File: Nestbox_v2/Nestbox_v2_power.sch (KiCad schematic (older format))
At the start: 27 parts, among them J201 BATT_CONN_01X02, Q201 Q_PMOS_DGS, U201 TPS62745, U202 LTC3534, U203 LP5907

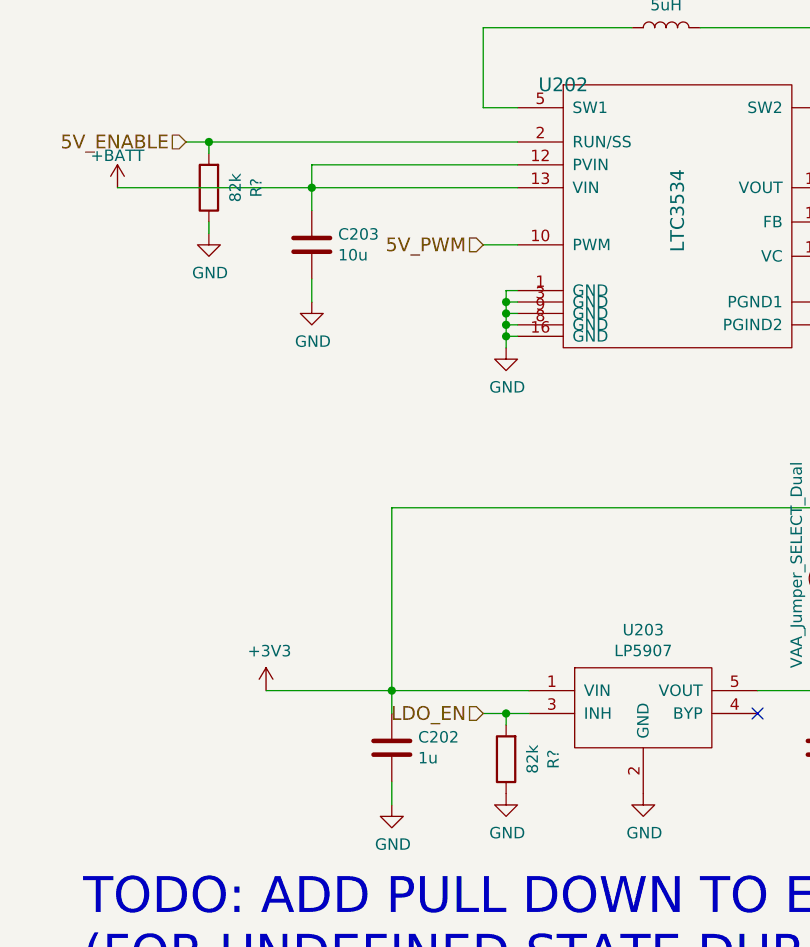
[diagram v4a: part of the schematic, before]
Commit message: TAPEOUT second batch nestbox main + EM pcb. added pull-ups, corrected pmos of load cell, WIFI AND SDCARD ENABLE PMOS ARE STILL WRONGLY ORIENTED
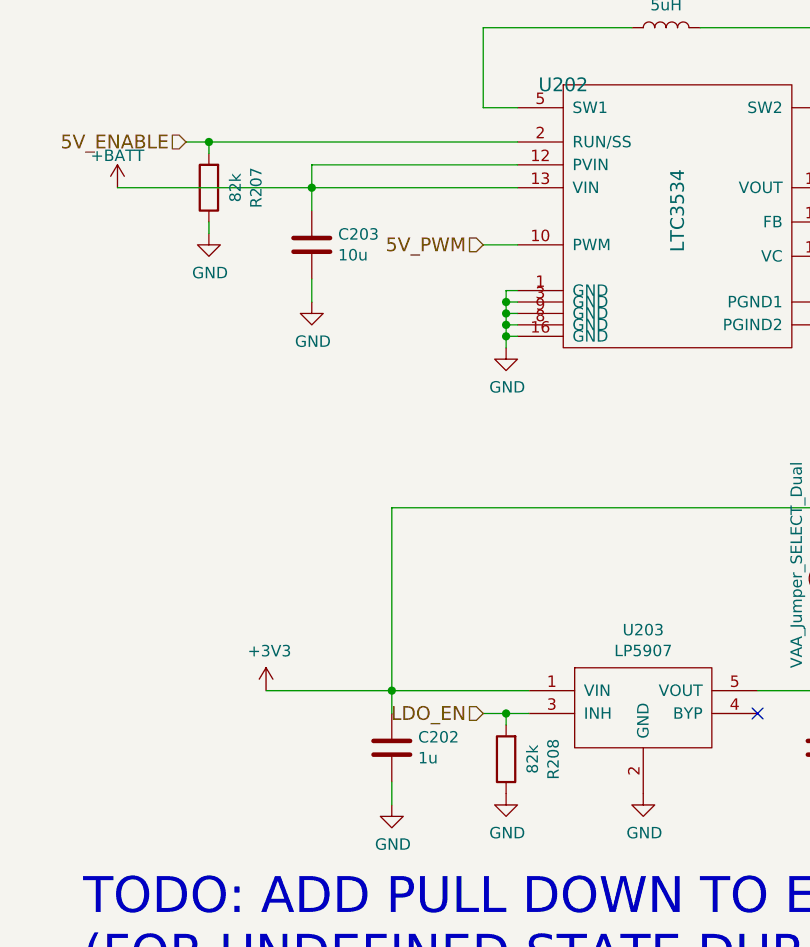
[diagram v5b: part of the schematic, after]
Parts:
- C201, C203, C205, C206, C207: footprint Capacitors_SMD:C_0603 -> Capacitors_SMD:C_0805
- gave numbers to parts that had none: 2
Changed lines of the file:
@@
 $EndComp
 $Comp
-L GND #PWR208
+L GND #PWR209
 U 1 1 5A0217A9
 P 3000 2550
-F 0 "#PWR208" H 3000 2300 50  0001 C CNN
+F 0 "#PWR209" H 3000 2300 50  0001 C CNN
 F 1 "GND" H 3005 2377 50  0000 C CNN
 F 2 "" H 3000 2550 50  0001 C CNN
@@
 F 0 "C201" H 1865 2196 50  0000 L CNN
 F 1 "10u" H 1865 2105 50  0000 L CNN
-F 2 "Capacitors_SMD:C_0603" H 1788 2000 50  0001 C CNN
+F 2 "Capacitors_SMD:C_0805" H 1788 2000 50  0001 C CNN
 F 3 "" H 1750 2150 50  0001 C CNN
 	1    1750 2150
@@
 $EndComp
 $Comp
-L GND #PWR203
+L GND #PWR204
 U 1 1 5A021A75
 P 1750 2400
-F 0 "#PWR203" H 1750 2150 50  0001 C CNN
+F 0 "#PWR204" H 1750 2150 50  0001 C CNN
 F 1 "GND" H 1755 2227 50  0000 C CNN
 F 2 "" H 1750 2400 50  0001 C CNN
@@
 $EndComp
 $Comp
-L +3.3V #PWR219
+L +3.3V #PWR221
 U 1 1 5A021DFB
 P 6750 1900
-F 0 "#PWR219" H 6750 1750 50  0001 C CNN
+F 0 "#PWR221" H 6750 1750 50  0001 C CNN
 F 1 "+3.3V" V 6765 2028 50  0000 L CNN
 F 2 "" H 6750 1900 50  0001 C CNN
@@
 $EndComp
 $Comp
-L GND #PWR209
+L GND #PWR210
 U 1 1 5A022A31
 P 3000 4850
-F 0 "#PWR209" H 3000 4600 50  0001 C CNN
+F 0 "#PWR210" H 3000 4600 50  0001 C CNN
 F 1 "GND" H 3005 4677 50  0000 C CNN
 F 2 "" H 3000 4850 50  0001 C CNN
@@
 F 0 "C203" H 2265 4446 50  0000 L CNN
 F 1 "10u" H 2265 4355 50  0000 L CNN
-F 2 "Capacitors_SMD:C_0603" H 2188 4250 50  0001 C CNN
+F 2 "Capacitors_SMD:C_0805" H 2188 4250 50  0001 C CNN
 F 3 "" H 2150 4400 50  0001 C CNN
 	1    2150 4400
@@
 $EndComp
 $Comp
-L GND #PWR205
+L GND #PWR206
 U 1 1 5A022A41
 P 2150 4650
-F 0 "#PWR205" H 2150 4400 50  0001 C CNN
+F 0 "#PWR206" H 2150 4400 50  0001 C CNN
 F 1 "GND" H 2155 4477 50  0000 C CNN
 F 2 "" H 2150 4650 50  0001 C CNN
@@
 $EndComp
 $Comp
-L +5V #PWR220
+L +5V #PWR222
 U 1 1 5A0232FE
 P 7600 4150
-F 0 "#PWR220" H 7600 4000 50  0001 C CNN
+F 0 "#PWR222" H 7600 4000 50  0001 C CNN
 F 1 "+5V" V 7615 4278 50  0000 L CNN
 F 2 "" H 7600 4150 50  0001 C CNN
@@
 F 0 "C206" H 6415 4446 50  0000 L CNN
 F 1 "10u" H 6415 4355 50  0000 L CNN
-F 2 "Capacitors_SMD:C_0603" H 6338 4250 50  0001 C CNN
+F 2 "Capacitors_SMD:C_0805" H 6338 4250 50  0001 C CNN
 F 3 "" H 6300 4400 50  0001 C CNN
 	1    6300 4400
@@
 F 0 "C207" H 6815 4446 50  0000 L CNN
 F 1 "10u" H 6815 4355 50  0000 L CNN
-F 2 "Capacitors_SMD:C_0603" H 6738 4250 50  0001 C CNN
+F 2 "Capacitors_SMD:C_0805" H 6738 4250 50  0001 C CNN
 F 3 "" H 6700 4400 50  0001 C CNN
 	1    6700 4400
@@
 $EndComp
 $Comp
-L GND #PWR218
+L GND #PWR220
 U 1 1 5A0246BF
 P 6500 4700
-F 0 "#PWR218" H 6500 4450 50  0001 C CNN
+F 0 "#PWR220" H 6500 4450 50  0001 C CNN
 F 1 "GND" H 6505 4527 50  0000 C CNN
 F 2 "" H 6500 4700 50  0001 C CNN
@@
 $EndComp
 $Comp
-L GND #PWR217
+L GND #PWR219
 U 1 1 5A0247CA
 P 5650 4800
-F 0 "#PWR217" H 5650 4550 50  0001 C CNN
+F 0 "#PWR219" H 5650 4550 50  0001 C CNN
 F 1 "GND" H 5655 4627 50  0000 C CNN
 F 2 "" H 5650 4800 50  0001 C CNN
@@
 F 0 "C205" H 5415 2196 50  0000 L CNN
 F 1 "10u" H 5415 2105 50  0000 L CNN
-F 2 "Capacitors_SMD:C_0603" H 5338 2000 50  0001 C CNN
+F 2 "Capacitors_SMD:C_0805" H 5338 2000 50  0001 C CNN
 F 3 "" H 5300 2150 50  0001 C CNN
 	1    5300 2150
@@
 $EndComp
 $Comp
-L GND #PWR216
+L GND #PWR218
 U 1 1 5A024E9A
 P 5300 2400
-F 0 "#PWR216" H 5300 2150 50  0001 C CNN
+F 0 "#PWR218" H 5300 2150 50  0001 C CNN
 F 1 "GND" H 5305 2227 50  0000 C CNN
 F 2 "" H 5300 2400 50  0001 C CNN
@@
 $EndComp
 $Comp
-L GND #PWR222
+L GND #PWR224
 U 1 1 5B072B3F
 P 8350 3150
-F 0 "#PWR222" H 8350 2900 50  0001 C CNN
+F 0 "#PWR224" H 8350 2900 50  0001 C CNN
 F 1 "GND" H 8350 3000 50  0000 C CNN
 F 2 "" H 8350 3150 50  0001 C CNN
@@
 $EndComp
 $Comp
-L +3V3 #PWR204
+L +3V3 #PWR205
 U 1 1 5B0757C4
 P 1950 6350
-F 0 "#PWR204" H 1950 6200 50  0001 C CNN
+F 0 "#PWR205" H 1950 6200 50  0001 C CNN
 F 1 "+3V3" H 1965 6523 50  0000 C CNN
 F 2 "" H 1950 6350 50  0001 C CNN
@@
 $EndComp
 $Comp
-L GND #PWR211
+L GND #PWR213
 U 1 1 5B0757CA
 P 3600 6800
-F 0 "#PWR211" H 3600 6550 50  0001 C CNN
+F 0 "#PWR213" H 3600 6550 50  0001 C CNN
 F 1 "GND" H 3605 6627 50  0000 C CNN
 F 2 "" H 3600 6800 50  0001 C CNN
@@
 NoConn ~ 4100 6450
 $Comp
-L VAA #PWR215
+L VAA #PWR217
 U 1 1 5B0757D1
 P 4700 5750
-F 0 "#PWR215" H 4700 5600 50  0001 C CNN
+F 0 "#PWR217" H 4700 5600 50  0001 C CNN
 F 1 "VAA" H 4717 5923 50  0000 C CNN
 F 2 "" H 4700 5750 50  0001 C CNN
@@
 $EndComp
 $Comp
-L GND #PWR207
+L GND #PWR208
 U 1 1 5B090D04
 P 2550 2950
-F 0 "#PWR207" H 2550 2700 50  0001 C CNN
+F 0 "#PWR208" H 2550 2700 50  0001 C CNN
 F 1 "GND" H 2555 2777 50  0000 C CNN
 F 2 "" H 2550 2950 50  0001 C CNN
@@
 $EndComp
 $Comp
-L GND #PWR206
+L GND #PWR207
 U 1 1 5B095296
 P 2500 6850
-F 0 "#PWR206" H 2500 6600 50  0001 C CNN
+F 0 "#PWR207" H 2500 6600 50  0001 C CNN
 F 1 "GND" H 2505 6677 50  0000 C CNN
 F 2 "" H 2500 6850 50  0001 C CNN
@@
 $EndComp
 $Comp
-L GND #PWR212
+L GND #PWR214
 U 1 1 5B095588
 P 4400 6800
-F 0 "#PWR212" H 4400 6550 50  0001 C CNN
+F 0 "#PWR214" H 4400 6550 50  0001 C CNN
 F 1 "GND" H 4405 6627 50  0000 C CNN
 F 2 "" H 4400 6800 50  0001 C CNN
@@
 $EndComp
 $Comp
-L +BATT #PWR221
+L +BATT #PWR223
 U 1 1 5B0B9A8C
 P 8200 3250
-F 0 "#PWR221" H 8200 3100 50  0001 C CNN
+F 0 "#PWR223" H 8200 3100 50  0001 C CNN
 F 1 "+BATT" H 8200 3390 50  0000 C CNN
 F 2 "" H 8200 3250 50  0001 C CNN
@@
 Connection ~ 4550 4450
 $Comp
-L GND #PWR213
+L GND #PWR215
 U 1 1 5B11A0A6
 P 4500 4900
-F 0 "#PWR213" H 4500 4650 50  0001 C CNN
+F 0 "#PWR215" H 4500 4650 50  0001 C CNN
 F 1 "GND" H 4505 4727 50  0000 C CNN
 F 2 "" H 4500 4900 50  0001 C CNN
@@
 	3000 2400 3050 2400
 $Comp
-L +BATT #PWR214
+L +BATT #PWR216
 U 1 1 5B14A10E
 P 4550 2100
-F 0 "#PWR214" H 4550 1950 50  0001 C CNN
+F 0 "#PWR216" H 4550 1950 50  0001 C CNN
 F 1 "+BATT" H 4550 2240 50  0000 C CNN
 F 2 "" H 4550 2100 50  0001 C CNN
@@
 	3600 2850 3600 2800
 $Comp
-L GND #PWR210
+L GND #PWR212
 U 1 1 5B18018D
 P 3500 2850
-F 0 "#PWR210" H 3500 2600 50  0001 C CNN
+F 0 "#PWR212" H 3500 2600 50  0001 C CNN
 F 1 "GND" H 3505 2677 50  0000 C CNN
 F 2 "" H 3500 2850 50  0001 C CNN
@@
 TODO: ADD PULL DOWN TO ENABLE PIN \n(FOR UNDEFINED STATE DURING FLASHING)
 $Comp
-L R R?
+L R R207
 U 1 1 5B28CE2A
 P 1700 4150
-F 0 "R?" V 1493 4150 50  0000 C CNN
+F 0 "R207" V 1493 4150 50  0000 C CNN
 F 1 "82k" V 1584 4150 50  0000 C CNN
 F 2 "Resistors_SMD:R_0603" V 1630 4150 50  0001 C CNN
@@
 Connection ~ 1700 3950
 $Comp
-L GND #PWR?
+L GND #PWR203
 U 1 1 5B28CF96
 P 1700 4350
-F 0 "#PWR?" H 1700 4100 50  0001 C CNN
+F 0 "#PWR203" H 1700 4100 50  0001 C CNN
 F 1 "GND" H 1705 4177 50  0000 C CNN
 F 2 "" H 1700 4350 50  0001 C CNN
@@
 	1700 4350 1700 4300
 $Comp
-L R R?
+L R R208
 U 1 1 5B28D28A
 P 3000 6650
-F 0 "R?" V 2793 6650 50  0000 C CNN
+F 0 "R208" V 2793 6650 50  0000 C CNN
 F 1 "82k" V 2884 6650 50  0000 C CNN
 F 2 "Resistors_SMD:R_0603" V 2930 6650 50  0001 C CNN
@@
 Connection ~ 3000 6450
 $Comp
-L GND #PWR?
+L GND #PWR211
 U 1 1 5B28D3DF
 P 3000 6800
-F 0 "#PWR?" H 3000 6550 50  0001 C CNN
+F 0 "#PWR211" H 3000 6550 50  0001 C CNN
 F 1 "GND" H 3005 6627 50  0000 C CNN
 F 2 "" H 3000 6800 50  0001 C CNN
